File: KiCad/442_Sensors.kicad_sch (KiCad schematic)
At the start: 9 parts, among them J1 Conn_01x06, U1 LSM6DSO32TR, U2 MS560702BA03-50, U3 CAM-M8C-0

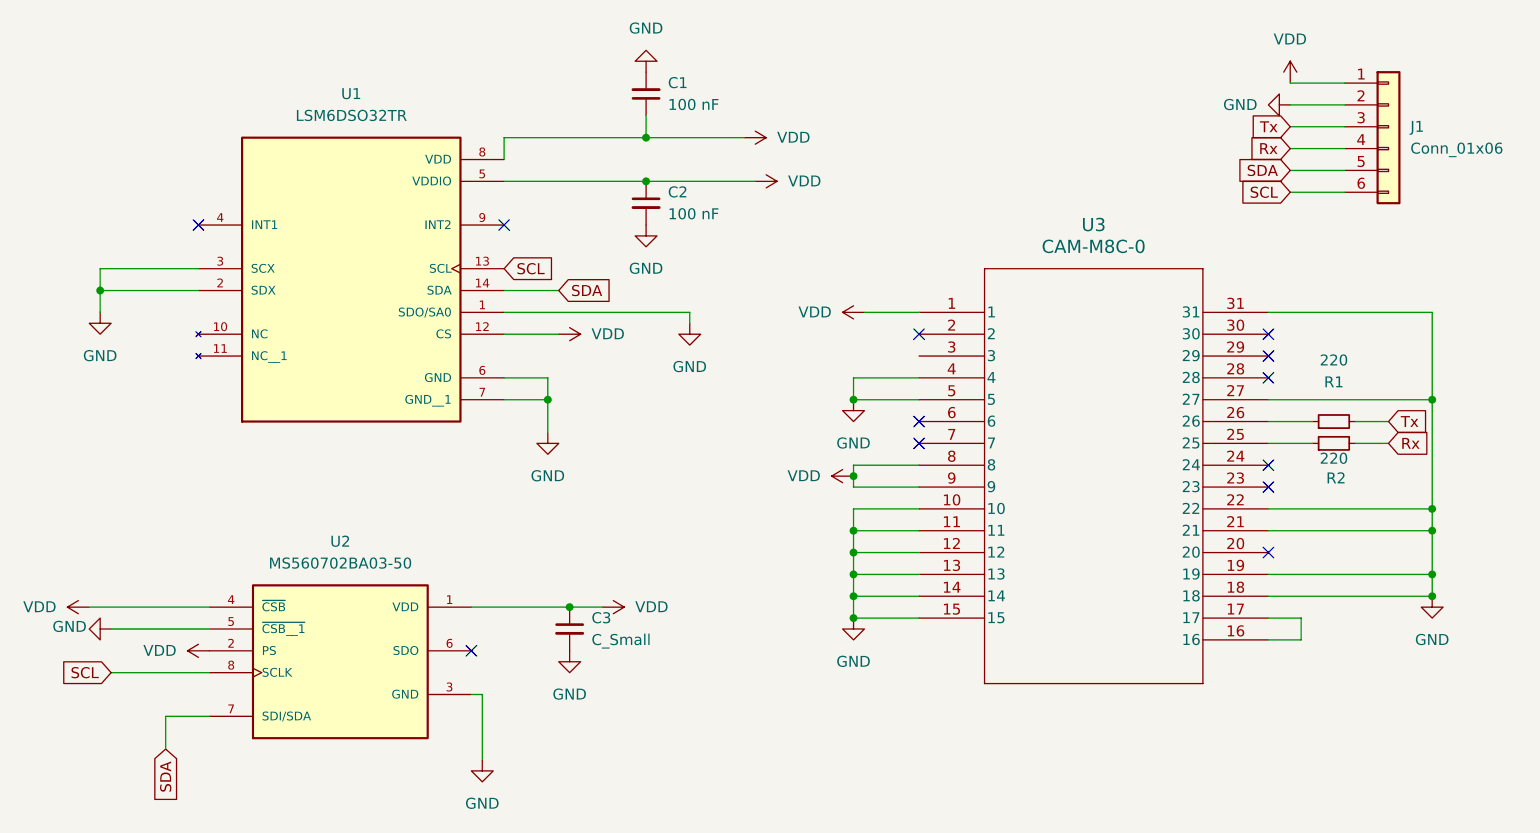
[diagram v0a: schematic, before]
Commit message: Added Sensors block
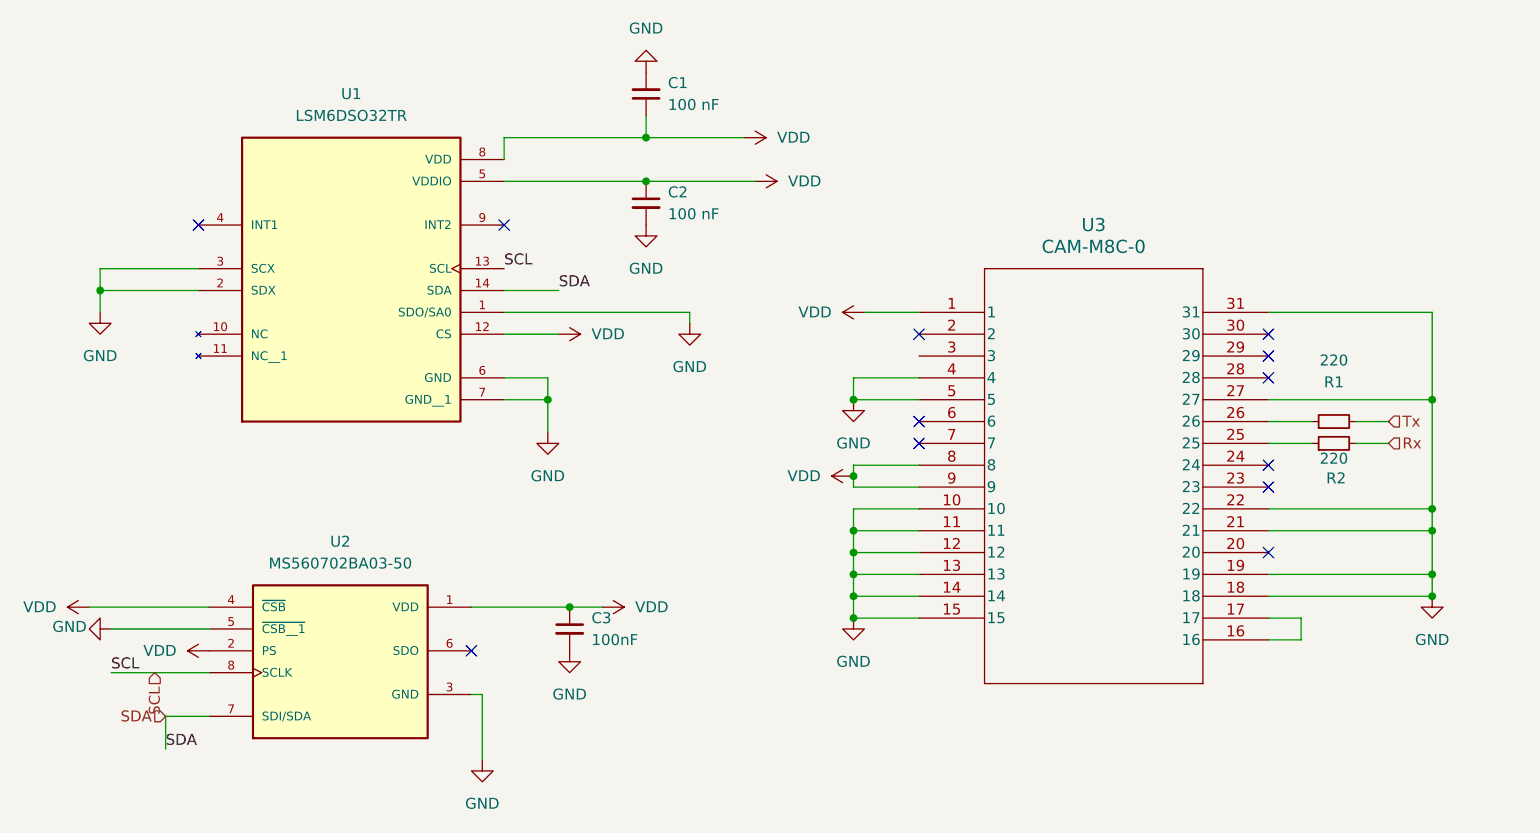
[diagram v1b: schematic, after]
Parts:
- removed J1: Conn_01x06, symbol Connector_Generic:Conn_01x06
- C3: value C_Small -> 100nF

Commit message: New GPS Module
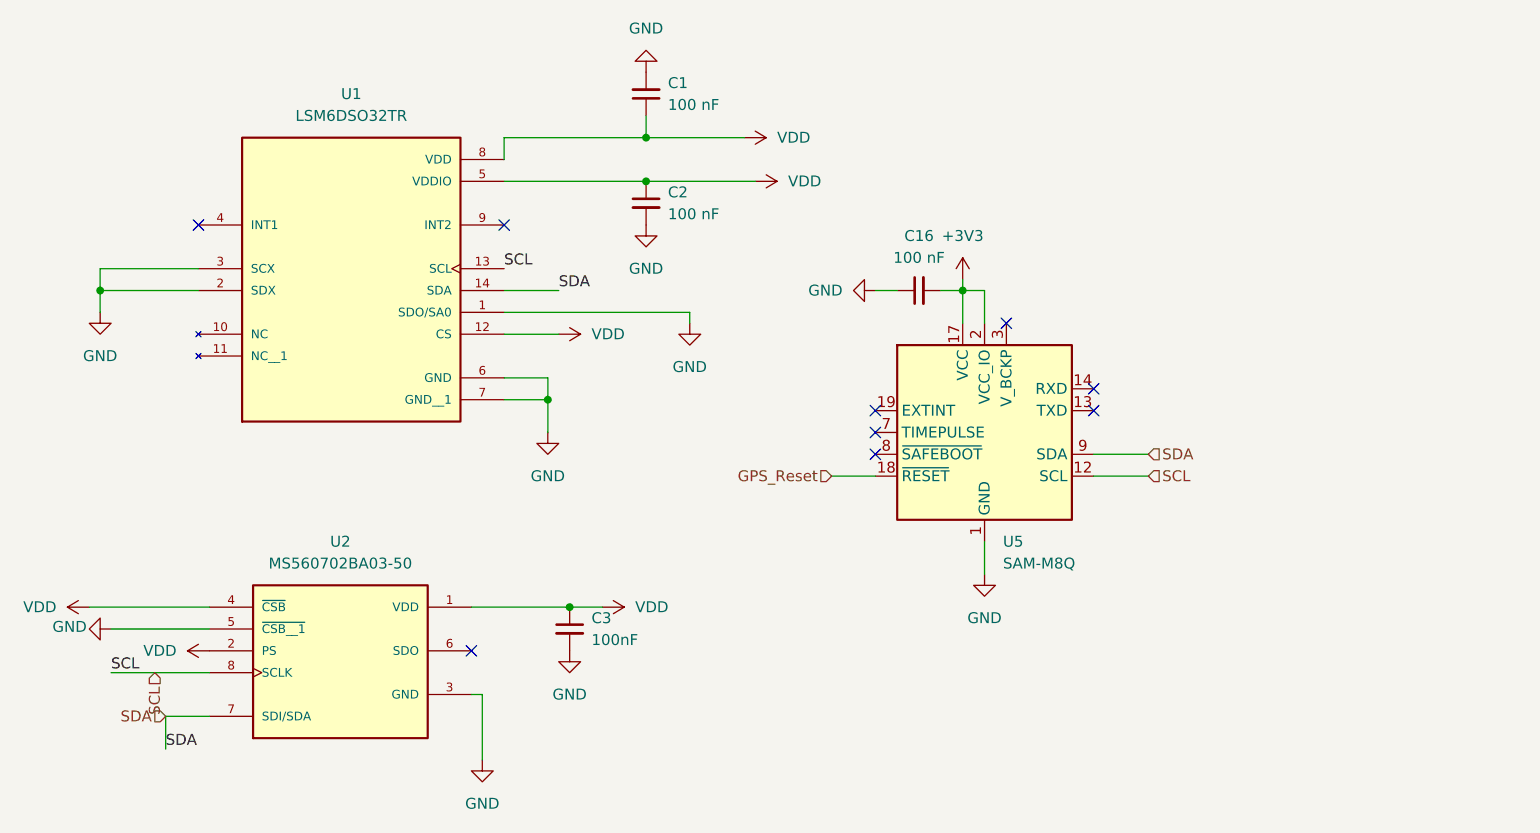
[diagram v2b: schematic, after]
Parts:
- removed R1, R2: 220, symbol Device:R_Small
- removed U3: CAM-M8C-0, QFN_M8C-0_UBL, symbol CAM-M8:CAM-M8C-0
- added C16: 100 nF, symbol Device:C_Small
- added U5: SAM-M8Q, RF_GPS:ublox_SAM-M8Q, symbol RF_GPS:SAM-M8Q
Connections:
- net GND: now also C16.1, U5.1 (GND), U5.10 (GND), U5.11 (GND), U5.15 (GND), U5.16 (GND), U5.20 (GND), U5.4 (GND), U5.5 (GND), U5.6 (GND)
- net SCL: now also U5.12 (SCL)
- net SDA: now also U5.9 (SDA)
- new net +3V3: C16.2, U5.17 (VCC), U5.2 (VCC_IO)
- new net GPS_Reset: U5.18 (~{RESET})
- no-connect marks 12 -> 9

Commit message: very rough sketch layout
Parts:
- C20: renamed from C3; footprint (none) -> Capacitor_SMD:C_0402_1005Metric
- C21: renamed from C1; footprint (none) -> Capacitor_SMD:C_0402_1005Metric
- C22: renamed from C2; footprint (none) -> Capacitor_SMD:C_0402_1005Metric
- C23: renamed from C16; footprint (none) -> Capacitor_SMD:C_0402_1005Metric
- U4: renamed from U2; footprint MS560702BA03-50:SON125P300X500X100-8N -> asdt-2:SON8_MS5611_TEC
- U5: renamed from U1; footprint LSM6DSO32TR:XDCR_LSM6DSO32TR -> Package_LGA:LGA-14_3x2.5mm_P0.5mm_LayoutBorder3x4y
- renumbered U5 to U6
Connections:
- net +3V3: now also C20.1, C21.1, C22.1, U4.1 (VDD), U4.2 (PS), U4.4 (~{CSB}), U5.5 (VDDIO), U5.8 (VDD)
- removed net VDD: C20.1, C21.1, C22.1, U4.1 (VDD), U4.2 (PS), U4.4 (~{CSB}), U5.12 (CS), U5.5 (VDDIO), U5.8 (VDD)
